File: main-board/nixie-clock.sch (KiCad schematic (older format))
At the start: 25 parts, among them P1 ESP8266_CONN, U1 STM32F103CBT6, Y1 32.768kHz

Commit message: #1 - stabilizator LDO AMS1117-3.3V
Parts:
- gave numbers to parts that had none: 17
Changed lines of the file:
@@
 	10600 2450 10850 2450
 $Comp
-L GND #PWR012
+L GND #PWR011
 U 1 1 5817B257
 P 10850 2450
-F 0 "#PWR012" H 10850 2200 50  0001 C CNN
+F 0 "#PWR011" H 10850 2200 50  0001 C CNN
 F 1 "GND" H 10850 2300 50  0000 C CNN
 F 2 "" H 10850 2450 50  0000 C CNN
@@
 $EndComp
 $Comp
-L VDD #PWR013
+L VDD #PWR012
 U 1 1 5817B5C8
 P 9800 2750
-F 0 "#PWR013" H 9800 2600 50  0001 C CNN
+F 0 "#PWR012" H 9800 2600 50  0001 C CNN
 F 1 "VDD" H 9800 2900 50  0000 C CNN
 F 2 "" H 9800 2750 50  0000 C CNN
@@
 	3900 6600 4450 6600
 $Comp
-L GND #PWR?
+L GND #PWR013
 U 1 1 5819F48F
 P 3300 7550
-F 0 "#PWR?" H 3300 7300 50  0001 C CNN
+F 0 "#PWR013" H 3300 7300 50  0001 C CNN
 F 1 "GND" H 3300 7400 50  0000 C CNN
 F 2 "" H 3300 7550 50  0000 C CNN
@@
 NMOD_SDA
 $Comp
-L PWR_FLAG #FLG?
+L PWR_FLAG #FLG014
 U 1 1 58212F70
 P 3400 1000
-F 0 "#FLG?" H 3400 1095 50  0001 C CNN
+F 0 "#FLG014" H 3400 1095 50  0001 C CNN
 F 1 "PWR_FLAG" H 3400 1180 50  0000 C CNN
 F 2 "" H 3400 1000 50  0000 C CNN
@@
 $EndComp
 $Comp
-L +5V #PWR?
+L +5V #PWR015
 U 1 1 58214622
 P 3250 700
-F 0 "#PWR?" H 3250 550 50  0001 C CNN
+F 0 "#PWR015" H 3250 550 50  0001 C CNN
 F 1 "+5V" H 3250 840 50  0000 C CNN
 F 2 "" H 3250 700 50  0000 C CNN
@@
 Connection ~ 3250 1000
 $Comp
-L +5V #PWR?
+L +5V #PWR016
 U 1 1 5821ADB1
 P 1650 6050
-F 0 "#PWR?" H 1650 5900 50  0001 C CNN
+F 0 "#PWR016" H 1650 5900 50  0001 C CNN
 F 1 "+5V" H 1650 6190 50  0000 C CNN
 F 2 "" H 1650 6050 50  0000 C CNN
@@
 $EndComp
 $Comp
-L R R?
+L R R2
 U 1 1 5822307D
 P 1300 6400
-F 0 "R?" V 1380 6400 50  0000 C CNN
+F 0 "R2" V 1380 6400 50  0000 C CNN
 F 1 "4k7" V 1300 6400 50  0000 C CNN
 F 2 "" V 1230 6400 50  0000 C CNN
@@
 $EndComp
 $Comp
-L R R?
+L R R1
 U 1 1 5822316A
 P 1000 6400
-F 0 "R?" V 1080 6400 50  0000 C CNN
+F 0 "R1" V 1080 6400 50  0000 C CNN
 F 1 "4k7" V 1000 6400 50  0000 C CNN
 F 2 "" V 930 6400 50  0000 C CNN
@@
 Connection ~ 1300 6150
 $Comp
-L GND #PWR?
+L GND #PWR017
 U 1 1 5822B6A3
 P 9950 3300
-F 0 "#PWR?" H 9950 3050 50  0001 C CNN
+F 0 "#PWR017" H 9950 3050 50  0001 C CNN
 F 1 "GND" H 9950 3150 50  0000 C CNN
 F 2 "" H 9950 3300 50  0000 C CNN
@@
 	9950 3150 9950 3300
 $Comp
-L L_Small L?
+L L_Small L1
 U 1 1 5823D1D2
 P 5950 1500
-F 0 "L?" H 5980 1540 50  0000 L CNN
+F 0 "L1" H 5980 1540 50  0000 L CNN
 F 1 "1u" H 5980 1460 50  0000 L CNN
 F 2 "" H 5950 1500 50  0000 C CNN
@@
 $EndComp
 $Comp
-L C C?
+L C C5
 U 1 1 5823DB5F
 P 4900 1650
-F 0 "C?" H 4925 1750 50  0000 L CNN
+F 0 "C5" H 4925 1750 50  0000 L CNN
 F 1 "100n" H 4925 1550 50  0000 L CNN
 F 2 "" H 4938 1500 50  0000 C CNN
@@
 $EndComp
 $Comp
-L C C?
+L C C6
 U 1 1 5823DCA3
 P 5150 1650
-F 0 "C?" H 5175 1750 50  0000 L CNN
+F 0 "C6" H 5175 1750 50  0000 L CNN
 F 1 "100n" H 5175 1550 50  0000 L CNN
 F 2 "" H 5188 1500 50  0000 C CNN
@@
 $EndComp
 $Comp
-L C C?
+L C C7
 U 1 1 5823DDC2
 P 5400 1650
-F 0 "C?" H 5425 1750 50  0000 L CNN
+F 0 "C7" H 5425 1750 50  0000 L CNN
 F 1 "100n" H 5425 1550 50  0000 L CNN
 F 2 "" H 5438 1500 50  0000 C CNN
@@
 $EndComp
 $Comp
-L C C?
+L C C9
 U 1 1 5823DE92
 P 6350 1650
-F 0 "C?" H 6375 1750 50  0000 L CNN
+F 0 "C9" H 6375 1750 50  0000 L CNN
 F 1 "10n" H 6375 1550 50  0000 L CNN
 F 2 "" H 6388 1500 50  0000 C CNN
@@
 $EndComp
 $Comp
-L GND #PWR?
+L GND #PWR018
 U 1 1 5823EC3A
 P 4900 1850
-F 0 "#PWR?" H 4900 1600 50  0001 C CNN
+F 0 "#PWR018" H 4900 1600 50  0001 C CNN
 F 1 "GND" H 4900 1700 50  0000 C CNN
 F 2 "" H 4900 1850 50  0000 C CNN
@@
 $EndComp
 $Comp
-L CP C?
+L CP C8
 U 1 1 5824062E
 P 5600 1650
-F 0 "C?" H 5625 1750 50  0000 L CNN
+F 0 "C8" H 5625 1750 50  0000 L CNN
 F 1 "10u" H 5625 1550 50  0000 L CNN
 F 2 "" H 5638 1500 50  0000 C CNN
@@
 $EndComp
 $Comp
-L GND #PWR?
+L GND #PWR019
 U 1 1 58241A1B
 P 6350 1850
-F 0 "#PWR?" H 6350 1600 50  0001 C CNN
+F 0 "#PWR019" H 6350 1600 50  0001 C CNN
 F 1 "GND" H 6350 1700 50  0000 C CNN
 F 2 "" H 6350 1850 50  0000 C CNN
@@
 $EndComp
 $Comp
-L CP_Small C?
+L CP_Small C10
 U 1 1 5821B579
 P 9950 3050
-F 0 "C?" H 9960 3120 50  0000 L CNN
+F 0 "C10" H 9960 3120 50  0000 L CNN
 F 1 "100u" H 9960 2970 50  0000 L CNN
 F 2 "" H 9950 3050 50  0000 C CNN
@@
 Connection ~ 5600 1500
 $Comp
-L GND #PWR?
+L GND #PWR020
 U 1 1 5822205E
 P 5800 5900
-F 0 "#PWR?" H 5800 5650 50  0001 C CNN
+F 0 "#PWR020" H 5800 5650 50  0001 C CNN
 F 1 "GND" H 5800 5750 50  0000 C CNN
 F 2 "" H 5800 5900 50  0000 C CNN
@@
 200VSENSE
 $Comp
-L ROTARY_ENCODER_SWITCH SW?
+L ROTARY_ENCODER_SWITCH SW1
 U 1 1 5827D24D
 P 10150 1300
-F 0 "SW?" H 10150 1560 50  0000 C CNN
+F 0 "SW1" H 10150 1560 50  0000 C CNN
 F 1 "ROTARY_ENCODER_SWITCH" H 10150 1040 50  0000 C CNN
 F 2 "" H 10050 1460 50  0001 C CNN
@@
 $EndComp
 $Comp
-L GND #PWR?
+L GND #PWR021
 U 1 1 58281FC0
 P 9450 1700
-F 0 "#PWR?" H 9450 1450 50  0001 C CNN
+F 0 "#PWR021" H 9450 1450 50  0001 C CNN
 F 1 "GND" H 9450 1550 50  0000 C CNN
 F 2 "" H 9450 1700 50  0000 C CNN
@@
 	9450 1300 9450 1700
 $Comp
-L R R?
+L R R5
 U 1 1 58287760
 P 9650 900
-F 0 "R?" V 9730 900 50  0000 C CNN
+F 0 "R5" V 9730 900 50  0000 C CNN
 F 1 "4k7" V 9650 900 50  0000 C CNN
 F 2 "" V 9580 900 50  0000 C CNN
@@
 $EndComp
 $Comp
-L R R?
+L R R4
 U 1 1 58289107
 P 9250 900
-F 0 "R?" V 9330 900 50  0000 C CNN
+F 0 "R4" V 9330 900 50  0000 C CNN
 F 1 "4k7" V 9250 900 50  0000 C CNN
 F 2 "" V 9180 900 50  0000 C CNN
@@
 B
 $Comp
-L R R?
+L R R6
 U 1 1 5829021F
 P 10800 900
-F 0 "R?" V 10880 900 50  0000 C CNN
+F 0 "R6" V 10880 900 50  0000 C CNN
 F 1 "4k7" V 10800 900 50  0000 C CNN
 F 2 "" V 10730 900 50  0000 C CNN
@@
 	10800 700  10800 750
 $Comp
-L C C?
+L C C11
 U 1 1 5829251C
 P 10950 1450
-F 0 "C?" H 10975 1550 50  0000 L CNN
+F 0 "C11" H 10975 1550 50  0000 L CNN
 F 1 "100n" H 10975 1350 50  0000 L CNN
 F 2 "" H 10988 1300 50  0000 C CNN
@@
 PRESS
 $Comp
-L CONN_01X06 P?
+L CONN_01X06 P2
 U 1 1 5829D2A4
 P 10500 5750
-F 0 "P?" H 10500 6100 50  0000 C CNN
+F 0 "P2" H 10500 6100 50  0000 C CNN
 F 1 "CONN_01X06" V 10600 5750 50  0000 C CNN
 F 2 "" H 10500 5750 50  0000 C CNN
@@
 $EndComp
 $Comp
-L GND #PWR?
+L GND #PWR022
 U 1 1 5829D7A9
 P 9850 6150
-F 0 "#PWR?" H 9850 5900 50  0001 C CNN
+F 0 "#PWR022" H 9850 5900 50  0001 C CNN
 F 1 "GND" H 9850 6000 50  0000 C CNN
 F 2 "" H 9850 6150 50  0000 C CNN
@@
 Connection ~ 9850 6000
 $Comp
-L VDD #PWR?
+L VDD #PWR023
 U 1 1 582A0114
 P 9250 700
-F 0 "#PWR?" H 9250 550 50  0001 C CNN
+F 0 "#PWR023" H 9250 550 50  0001 C CNN
 F 1 "VDD" H 9250 850 50  0000 C CNN
 F 2 "" H 9250 700 50  0000 C CNN
@@
 $EndComp
 $Comp
-L VDD #PWR?
+L VDD #PWR024
 U 1 1 582A0479
 P 10100 5350
-F 0 "#PWR?" H 10100 5200 50  0001 C CNN
+F 0 "#PWR024" H 10100 5200 50  0001 C CNN
 F 1 "VDD" H 10100 5500 50  0000 C CNN
 F 2 "" H 10100 5350 50  0000 C CNN
@@
 SWDCLK
 $Comp
-L C C?
+L C C4
 U 1 1 582A7AF0
 P 2550 2400
-F 0 "C?" H 2575 2500 50  0000 L CNN
+F 0 "C4" H 2575 2500 50  0000 L CNN
 F 1 "100n" H 2575 2300 50  0000 L CNN
 F 2 "" H 2588 2250 50  0000 C CNN
@@
 $EndComp
 $Comp
-L GND #PWR?
+L GND #PWR025
 U 1 1 582A7C03
 P 2550 2600
-F 0 "#PWR?" H 2550 2350 50  0001 C CNN
+F 0 "#PWR025" H 2550 2350 50  0001 C CNN
 F 1 "GND" H 2550 2450 50  0000 C CNN
 F 2 "" H 2550 2600 50  0000 C CNN
@@
 $EndComp
 $Comp
-L R R?
+L R R3
 U 1 1 582A7E8D
 P 2300 2150
-F 0 "R?" V 2380 2150 50  0000 C CNN
+F 0 "R3" V 2380 2150 50  0000 C CNN
 F 1 "10k" V 2300 2150 50  0000 C CNN
 F 2 "" V 2230 2150 50  0000 C CNN
@@
 $EndComp
 $Comp
-L VDD #PWR?
+L VDD #PWR026
 U 1 1 582A7F9C
 P 2000 2150
-F 0 "#PWR?" H 2000 2000 50  0001 C CNN
+F 0 "#PWR026" H 2000 2000 50  0001 C CNN
 F 1 "VDD" H 2000 2300 50  0000 C CNN
 F 2 "" H 2000 2150 50  0000 C CNN
@@
 RST
 $Comp
-L GND #PWR?
+L GND #PWR027
 U 1 1 582ABAFC
 P 2950 2650
-F 0 "#PWR?" H 2950 2400 50  0001 C CNN
+F 0 "#PWR027" H 2950 2400 50  0001 C CNN
 F 1 "GND" H 2950 2500 50  0000 C CNN
 F 2 "" H 2950 2650 50  0000 C CNN

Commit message: Polaczenie masy wyjscia ROM-1205S z masa 200V (-Vin z -Vout)
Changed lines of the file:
@@
 Wire Wire Line
 	2950 2650 3100 2650
+Wire Wire Line
+	2650 1450 3500 1450
+Connection ~ 3500 1450
 $EndSCHEMATC

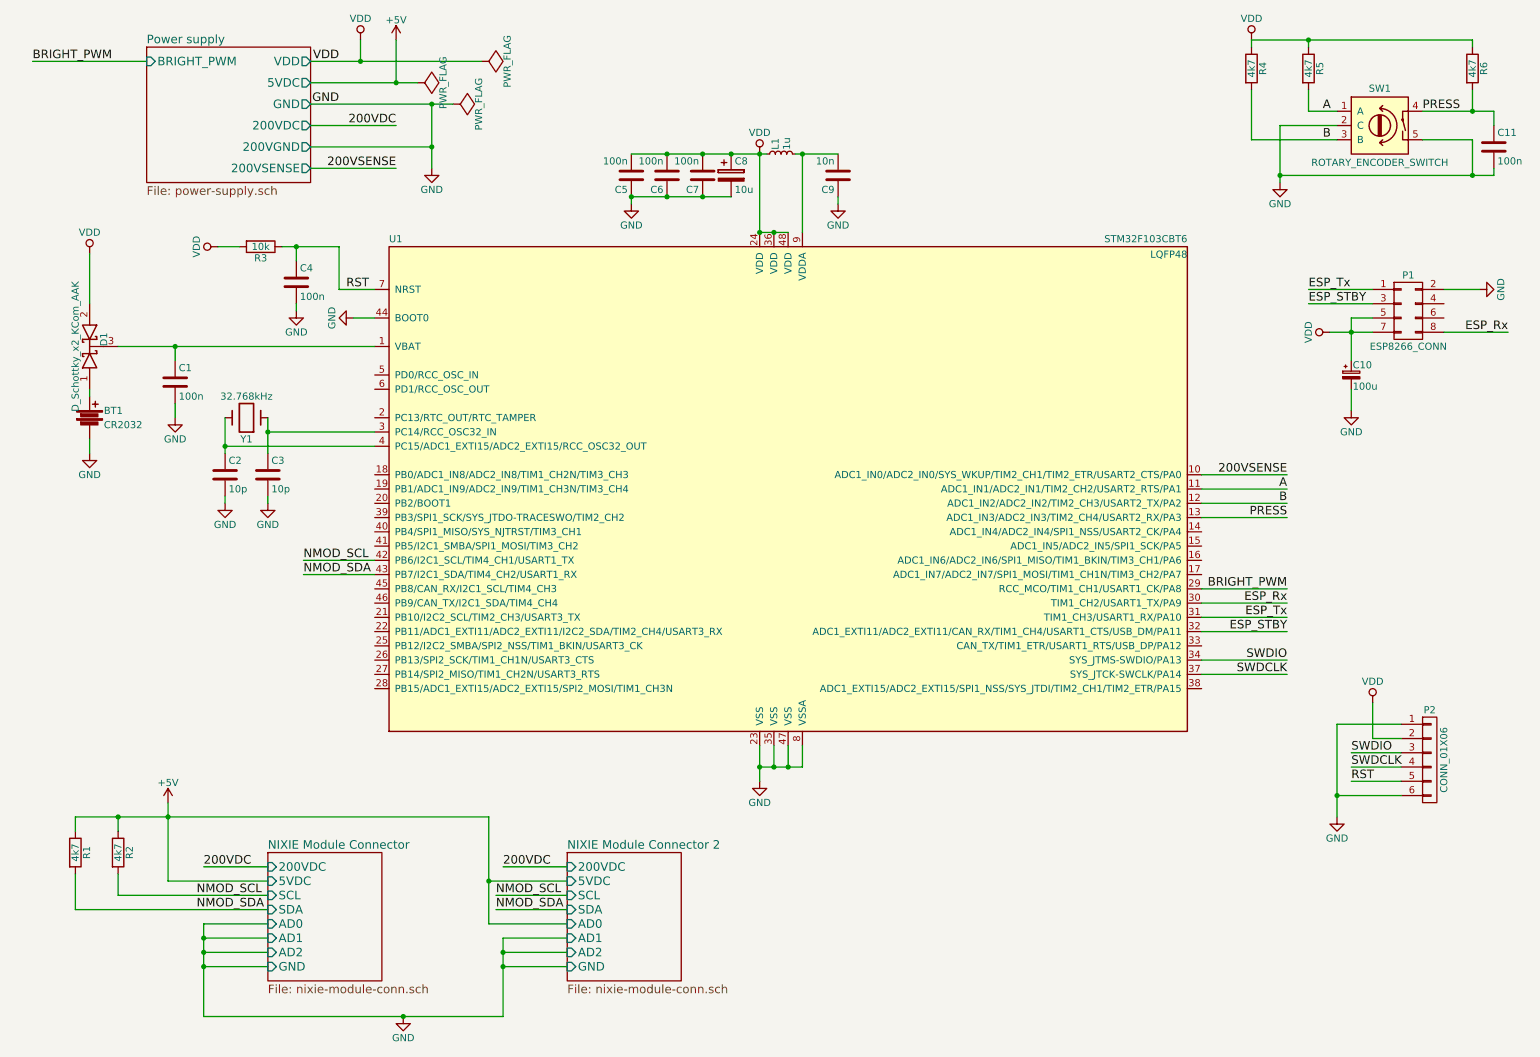
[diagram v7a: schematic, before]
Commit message: #1 - Poprawienie otoczenia ukladow od zasilania; tolerancja 1% rezystorow dzielnika pomiarowego; usuniecie kondensatora filtrujacego wyjscie z enkodera; oddalenie od siebie linii (przeniesienie 200VSENSE i BRIGHTPWM); odseparowanie I2C podciagnietej do 3,3V i 5V (po stronie GPIO Expandera) MOSFETami
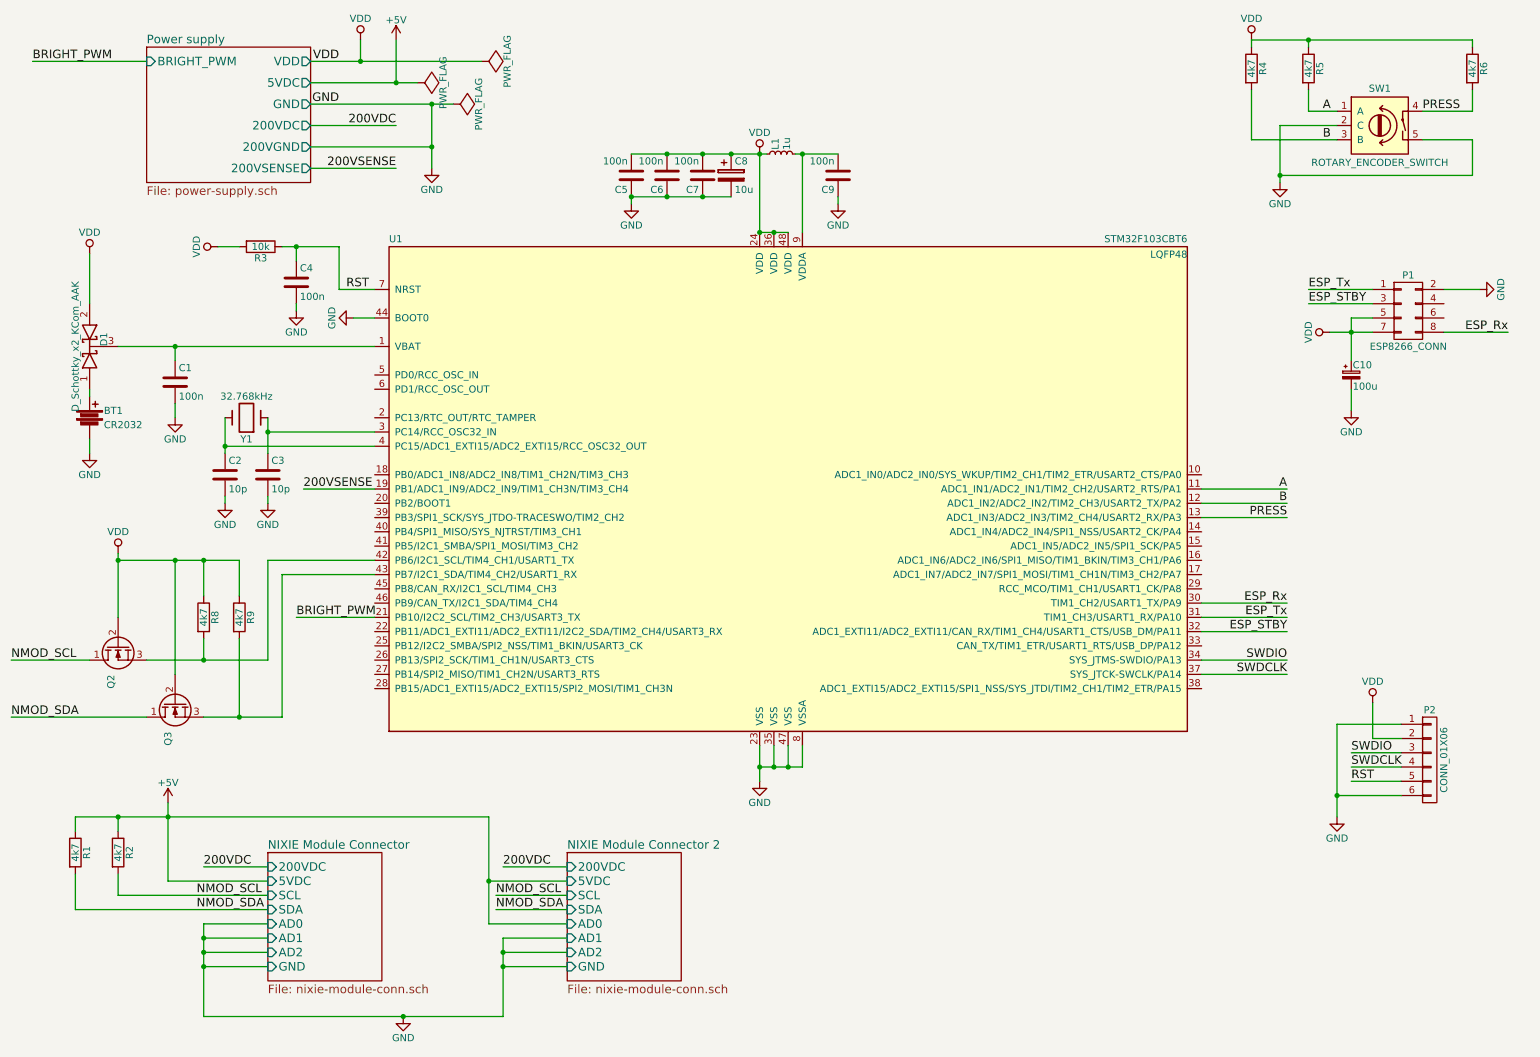
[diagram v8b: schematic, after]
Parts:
- removed C11: 100n, symbol C
- added Q2, Q3: Q_NMOS_DGS, symbol Q_NMOS_DGS
- added R8, R9: 4k7, symbol R
- C9: value 10n -> 100n
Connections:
- net 200VSENSE: now also U1.19 (PB1/ADC1_IN9/ADC2_IN9/TIM1_CH3N/TIM3_CH4); no longer U1.10 (ADC1_IN0/ADC2_IN0/SYS_WKUP/TIM2_CH1/TIM2_ETR/USART2_CTS/PA0)
- net BRIGHT_PWM: now also U1.21 (PB10/I2C2_SCL/TIM2_CH3/USART3_TX); no longer U1.29 (RCC_MCO/TIM1_CH1/USART1_CK/PA8)
- net NMOD_SCL: now also Q2.1 (D); no longer U1.42 (PB6/I2C1_SCL/TIM4_CH1/USART1_TX)
- net NMOD_SDA: now also Q3.1 (D); no longer U1.43 (PB7/I2C1_SDA/TIM4_CH2/USART1_RX)
- net VDD: now also Q2.2 (G), Q3.2 (G), R8.1, R9.1
- new net: Q2.3 (S), R8.2, U1.42 (PB6/I2C1_SCL/TIM4_CH1/USART1_TX)
- new net: Q3.3 (S), R9.2, U1.43 (PB7/I2C1_SDA/TIM4_CH2/USART1_RX)
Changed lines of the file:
@@
 Text Label 9650 2550 0    60   ~ 0
 ESP_STBY
-Wire Wire Line
-	8900 4550 9500 4550
-Text Label 9500 4550 2    60   ~ 0
+Text Label 2550 4750 0    60   ~ 0
 BRIGHT_PWM
 Wire Wire Line
@@
 Connection ~ 4000 7100
 Wire Wire Line
-	2600 4350 3100 4350
-Wire Wire Line
-	2600 4450 3100 4450
-Text Label 2600 4350 0    60   ~ 0
+	2350 4350 3100 4350
+Wire Wire Line
+	2450 4450 3100 4450
+Text Label 550  5050 0    60   ~ 0
 NMOD_SCL
-Text Label 2600 4450 0    60   ~ 0
+Text Label 550  5450 0    60   ~ 0
 NMOD_SDA
 Wire Wire Line
@@
 P 6350 1650
 F 0 "C9" H 6375 1750 50  0000 L CNN
-F 1 "10n" H 6375 1550 50  0000 L CNN
+F 1 "100n" H 6375 1550 50  0000 L CNN
 F 2 "" H 6388 1500 50  0000 C CNN
 F 3 "" H 6350 1650 50  0000 C CNN
@@
 Text Label 3250 1600 2    60   ~ 0
 200VSENSE
-Wire Wire Line
-	8900 3750 9500 3750
-Text Label 9500 3750 2    60   ~ 0
+Text Label 2600 3850 0    60   ~ 0
 200VSENSE
 $Comp
@@
 $EndComp
 Wire Wire Line
-	10450 1200 10950 1200
-Wire Wire Line
 	10800 1200 10800 1050
 Connection ~ 9650 700
 Wire Wire Line
-	9450 1650 10950 1650
-Wire Wire Line
 	10800 1650 10800 1400
 Wire Wire Line
 	10800 1400 10450 1400
-Connection ~ 9450 1650
 Text Label 10450 1200 0    60   ~ 0
 PRESS
 Wire Wire Line
 	10800 700  10800 750
-$Comp
-L C C11
-U 1 1 5829251C
-P 10950 1450
-F 0 "C11" H 10975 1550 50  0000 L CNN
-F 1 "100n" H 10975 1350 50  0000 L CNN
-F 2 "" H 10988 1300 50  0000 C CNN
-F 3 "" H 10950 1450 50  0000 C CNN
-	1    10950 1450
-	1    0    0    -1
-$EndComp
-Wire Wire Line
-	10950 1650 10950 1600
-Connection ~ 10800 1650
-Wire Wire Line
-	10950 1200 10950 1300
-Connection ~ 10800 1200
 Wire Wire Line
 	8900 3850 9500 3850
@@
 	2650 1450 3500 1450
 Connection ~ 3500 1450
+Wire Wire Line
+	10800 1650 9450 1650
+Connection ~ 9450 1650
+Wire Wire Line
+	10800 1200 10450 1200
+Wire Wire Line
+	2600 3850 3100 3850
+Wire Wire Line
+	2550 4750 3100 4750
+$Comp
+L VDD #PWR?
+U 1 1 58311767
+P 1300 4300
+F 0 "#PWR?" H 1300 4150 50  0001 C CNN
+F 1 "VDD" H 1300 4450 50  0000 C CNN
+F 2 "" H 1300 4300 50  0000 C CNN
+F 3 "" H 1300 4300 50  0000 C CNN
+	1    1300 4300
+	1    0    0    -1
+$EndComp
+$Comp
+L Q_NMOS_DGS Q2
+U 1 1 583161E1
+P 1300 4950
+F 0 "Q2" H 1600 5000 50  0000 R CNN
+F 1 "Q_NMOS_DGS" H 1950 4900 50  0001 R CNN
+F 2 "" H 1500 5050 50  0000 C CNN
+F 3 "" H 1300 4950 50  0000 C CNN
+	1    1300 4950
+	0    -1   1    0
+$EndComp
+$Comp
+L Q_NMOS_DGS Q3
+U 1 1 583163F0
+P 1700 5350
+F 0 "Q3" H 2000 5400 50  0000 R CNN
+F 1 "Q_NMOS_DGS" H 2350 5300 50  0001 R CNN
+F 2 "" H 1900 5450 50  0000 C CNN
+F 3 "" H 1700 5350 50  0000 C CNN
+	1    1700 5350
+	0    -1   1    0
+$EndComp
+Wire Wire Line
+	1300 4750 1300 4300
+Wire Wire Line
+	1700 5150 1700 4350
+Wire Wire Line
+	1300 4350 2150 4350
+Connection ~ 1300 4350
+Wire Wire Line
+	550  5050 1100 5050
+Wire Wire Line
+	550  5450 1500 5450
+$Comp
+L R R8
+U 1 1 58316CD4
+P 1900 4750
+F 0 "R8" V 1980 4750 50  0000 C CNN
+F 1 "4k7" V 1900 4750 50  0000 C CNN
+F 2 "" V 1830 4750 50  0000 C CNN
+F 3 "" H 1900 4750 50  0000 C CNN
+	1    1900 4750
+	1    0    0    -1
+$EndComp
+$Comp
+L R R9
+U 1 1 58316DFA
+P 2150 4750
+F 0 "R9" V 2230 4750 50  0000 C CNN
+F 1 "4k7" V 2150 4750 50  0000 C CNN
+F 2 "" V 2080 4750 50  0000 C CNN
+F 3 "" H 2150 4750 50  0000 C CNN
+	1    2150 4750
+	1    0    0    -1
+$EndComp
+Wire Wire Line
+	1500 5050 2350 5050
+Wire Wire Line
+	1900 5050 1900 4900
+Wire Wire Line
+	1900 5450 2450 5450
+Wire Wire Line
+	2150 5450 2150 4900
+Wire Wire Line
+	1900 4350 1900 4600
+Connection ~ 1700 4350
+Wire Wire Line
+	2150 4350 2150 4600
+Connection ~ 1900 4350
+Wire Wire Line
+	2350 5050 2350 4350
+Connection ~ 1900 5050
+Wire Wire Line
+	2450 5450 2450 4450
+Connection ~ 2150 5450
 $EndSCHEMATC
